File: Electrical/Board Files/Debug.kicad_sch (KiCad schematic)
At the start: 16 parts

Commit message: Updating for 3v3 operation
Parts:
- C?: value C_Small -> 1u
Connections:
- net +3V0 renamed +3V3
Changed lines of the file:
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@@
     (effects (font (size 1.27 1.27)) (justify left bottom))
   )
-  (hierarchical_label "SWD_CLK" (shape input) (at 61.595 113.665 0)
-    (effects (font (size 1.27 1.27)) (justify left))
-  )
-  (hierarchical_label "FTDI_TX" (shape input) (at 225.425 77.47 0)
+  (hierarchical_label "SWD_CLK" (shape output) (at 61.595 113.665 0)
+    (effects (font (size 1.27 1.27)) (justify left))
+  )
+  (hierarchical_label "FTDI_TX" (shape output) (at 225.425 77.47 0)
     (effects (font (size 1.27 1.27)) (justify left))
   )
@@
     (effects (font (size 1.27 1.27)) (justify left))
   )
-  (hierarchical_label "SWD_DATA" (shape input) (at 61.595 111.125 0)
+  (hierarchical_label "SWD_DATA" (shape bidirectional) (at 61.595 111.125 0)
     (effects (font (size 1.27 1.27)) (justify left))
   )
@@
     (pin "1")
   )
-  (symbol (lib_id "power:+3V0") (at 59.055 104.775 0) (unit 1)
-    (in_bom yes) (on_board yes) (fields_autoplaced)
-    (property "Reference" "#PWR?" (id 0) (at 59.055 108.585 0)
-      (effects (font (size 1.27 1.27)) hide)
-    )
-    (property "Value" "+3V0" (id 1) (at 59.055 99.949 0))
-    (property "Footprint" "" (id 2) (at 59.055 104.775 0)
-      (effects (font (size 1.27 1.27)) hide)
-    )
-    (property "Datasheet" "" (id 3) (at 59.055 104.775 0)
-      (effects (font (size 1.27 1.27)) hide)
-    )
-    (pin "1")
-  )
   (symbol (lib_id "Device:R_Small_US") (at 125.095 87.63 90) (unit 1)
     (in_bom yes) (on_board yes)
@@
     (pin "2")
   )
+  (symbol (lib_id "power:+3V3") (at 59.055 104.775 0) (unit 1)
+    (in_bom yes) (on_board yes) (fields_autoplaced)
+    (property "Reference" "#PWR?" (id 0) (at 59.055 108.585 0)
+      (effects (font (size 1.27 1.27)) hide)
+    )
+    (property "Value" "+3V3" (id 1) (at 59.055 100.203 0))
+    (property "Footprint" "" (id 2) (at 59.055 104.775 0)
+      (effects (font (size 1.27 1.27)) hide)
+    )
+    (property "Datasheet" "" (id 3) (at 59.055 104.775 0)
+      (effects (font (size 1.27 1.27)) hide)
+    )
+    (pin "1")
+  )
   (symbol (lib_id "Device:C_Small") (at 135.89 111.125 0) (unit 1)
     (in_bom yes) (on_board yes) (fields_autoplaced)
-    (property "Reference" "C?" (id 0) (at 139.065 109.8612 0)
-      (effects (font (size 1.27 1.27)) (justify left))
-    )
-    (property "Value" "C_Small" (id 1) (at 139.065 112.4012 0)
-      (effects (font (size 1.27 1.27)) (justify left))
-    )
+    (property "Reference" "C?" (id 0) (at 138.43 109.8612 0)
+      (effects (font (size 1.27 1.27)) (justify left))
+    )
+    (property "Value" "1u" (id 1) (at 138.43 112.4012 0)
+      (effects (font (size 1.27 1.27)) (justify left))
+    )

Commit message: Added Xbee libs and bus aliases
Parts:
- gave numbers to parts that had none: 16
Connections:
- net FTDI_RX renamed FUART.TX
- net FTDI_TX renamed FUART.RX
- net SWD_CLK renamed SWD.CLK
- net SWD_DATA renamed SWD.DATA
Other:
- title: (none) -> Robotics Controller
- moved on the sheet: C36, D19, D20, J2, J3, R22, R23, R24, R25, TP15, TP16, TP17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

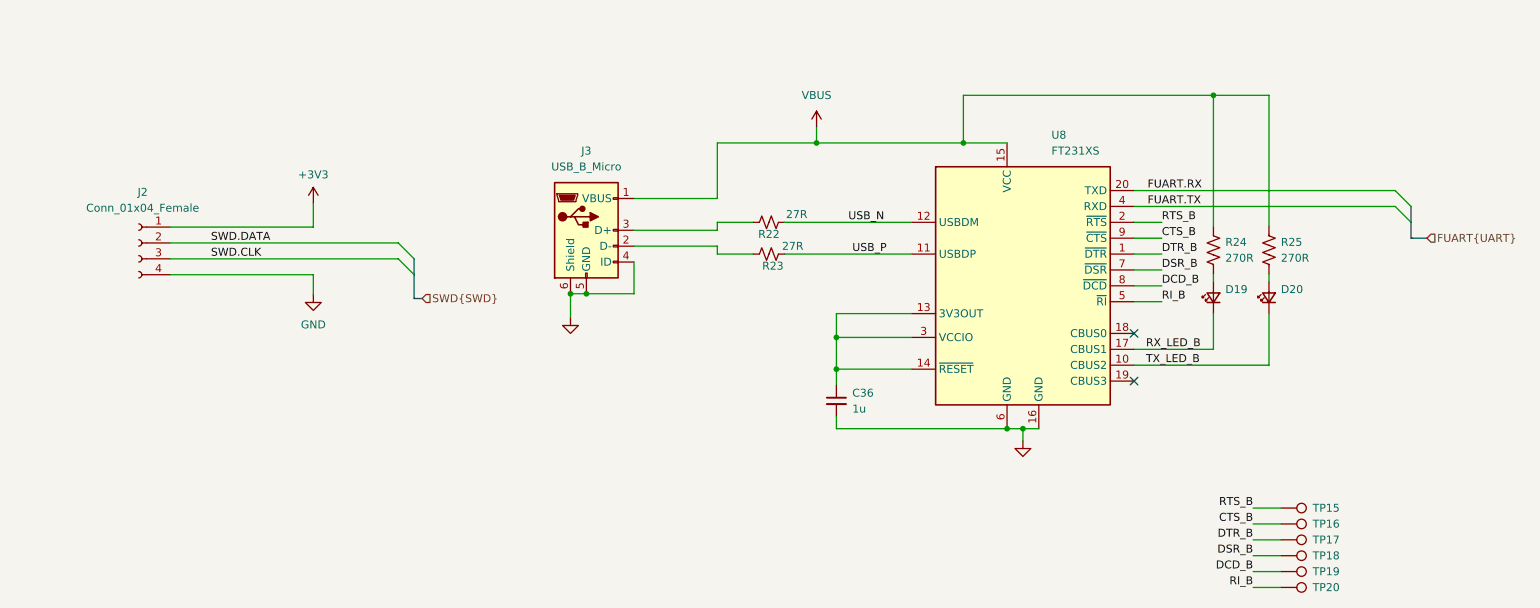
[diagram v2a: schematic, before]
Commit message: Added hall effect sensors
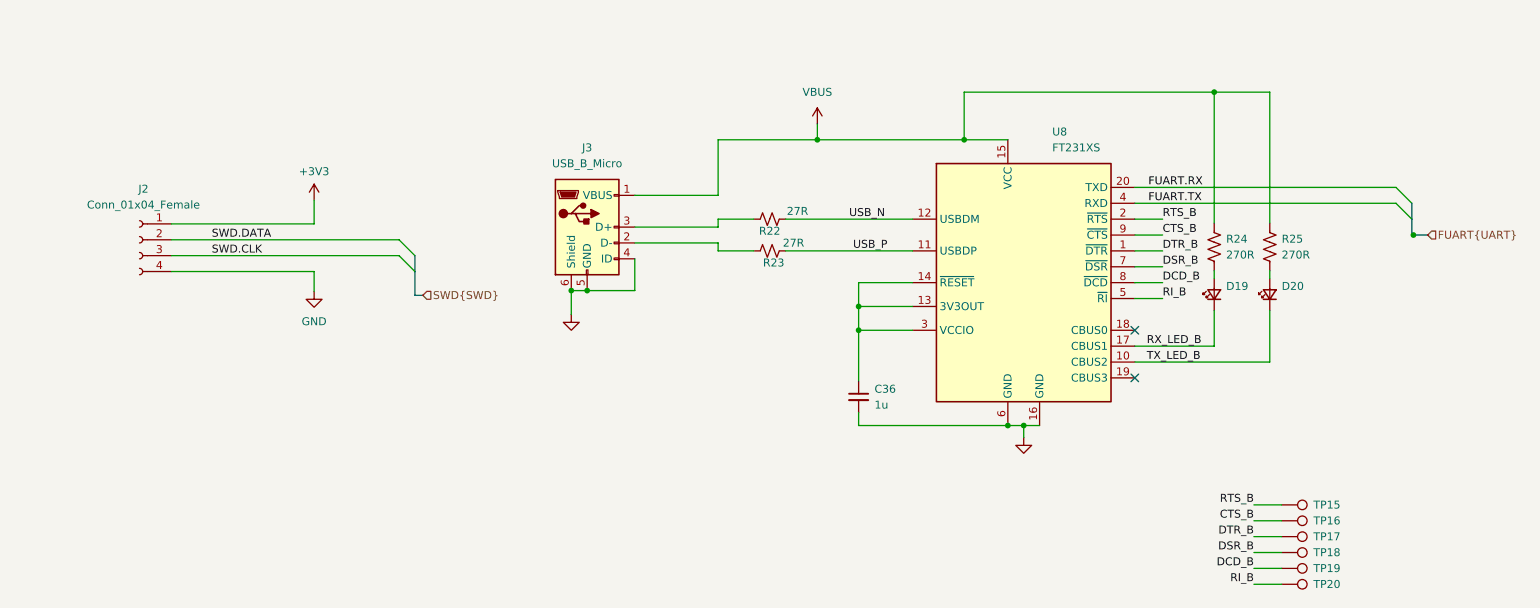
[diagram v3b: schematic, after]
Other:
- moved on the sheet: C36, D19, D20, J2, J3, R22, R23, R24, R25, TP15, TP16, TP17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

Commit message: Updating title block fields and adding pdf schematic
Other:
- company: (none) -> Rockerbotics
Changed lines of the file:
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@@
   (title_block
     (title "Robotics Controller")
+    (date "2022-09-02")
     (rev "A")
+    (company "Rockerbotics")
   )
   (junction (at 213.106 73.66) (diameter 0) (color 0 0 0 0)
